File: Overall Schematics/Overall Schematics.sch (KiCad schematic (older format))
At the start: 33 parts, among them J1 WattMeter1_Output, J2 WattMeter2_Output, J3 Intel_Buck_Converter_Input, J4 WattMeter1_Input, J5 WattMeter2_Input, M1 Stepper_Motor_bipolar, M10 Motor_Servo, M11 Stepper_Motor_bipolar, M12 Motor_Servo, M2 Stepper_Motor_bipolar, M3 LinActuator12V, M4 LinActuator12V, M5 LinActuator12V, M6 Motor_DC, M7 Motor_DC, M8 Motor_DC, M9 Motor_DC, SW1 SW_DPST, U1 Teensy4.1, U10 VNH52019, U11 ServoDriver, U12 36v4SMD, U13 D24V22F5, U2 36v4SMD, U3 36v4SMD, U4 VNH52019, U5 VNH52019, U6 VNH52019, U7 VNH52019, U8 VNH52019, U9 VNH52019

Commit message: PCB is basically done, going to check stuff again before ordering though
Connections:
- net Battery2_Positive is gone; now on net Battery2_Positive24V: J3.1 (Pin_1)
- net Battery1_Positive24V: now also U12.17 (VIN), U12.18 (VIN2), U5.14 (VIN(5.5V-24V)); no longer U10.14 (VIN(5.5V-24V)), U3.17 (VIN), U3.18 (VIN2)
- net Battery2_Positive24V: now also U10.14 (VIN(5.5V-24V)), U3.17 (VIN), U3.18 (VIN2); no longer U12.17 (VIN), U12.18 (VIN2), U5.14 (VIN(5.5V-24V))
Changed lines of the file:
@@
 	20950 12700 21050 12700
-$Comp
-L power:+3V3 #PWR0105
-U 1 1 5FAD46F5
-P 21050 12800
-F 0 "#PWR0105" H 21050 12650 50  0001 C CNN
-F 1 "+3V3" V 21065 12928 50  0000 L CNN
-F 2 "" H 21050 12800 50  0001 C CNN
-F 3 "" H 21050 12800 50  0001 C CNN
-	1    21050 12800
-	0    1    1    0
-$EndComp
-Wire Wire Line
-	20950 12800 21050 12800
 $Comp
 L power:+3V3 #PWR0106
@@
 Text GLabel 27400 15250 2    20   Input ~ 0
 Battery2_Positive24V
-Text GLabel 28750 14750 0    39   Input ~ 0
-Battery2_Positive
 Text GLabel 28550 12700 2    39   Input ~ 0
-Battery1_Positive24V
+Battery2_Positive24V
 Wire Wire Line
 	28400 11850 28550 11850
 Text GLabel 28550 11850 2    39   Input ~ 0
 Battery1_Positive24V
-Text GLabel 28550 11050 2    39   Input ~ 0
-Battery2_Positive24V
 Text GLabel 23600 11600 2    39   Input ~ 0
-Battery1_Positive24V
-Text GLabel 23550 10550 2    39   Input ~ 0
-Battery2_Positive24V
-Text GLabel 28550 10350 2    39   Input ~ 0
 Battery2_Positive24V
 Text GLabel 29500 9650 1    31   Input ~ 0
@@
 Battery1_Positive24V
 Text GLabel 23700 16750 2    39   Input ~ 0
-Battery2_Positive24V
+Battery1_Positive24V
 Wire Wire Line
 	23600 15400 23600 15500
@@
 	23600 9500 23600 9450
 Text GLabel 23600 9450 2    20   Input ~ 0
-Battery2_Positive24V
+Battery1_Positive24V
 Text GLabel 23600 9600 2    20   Input ~ 0
 PWR_GND
@@
 	0    1    1    0
 $EndComp
+$Comp
+L power:+3V3 #PWR0105
+U 1 1 602D660B
+P 21250 12800
+F 0 "#PWR0105" H 21250 12650 50  0001 C CNN
+F 1 "+3V3" H 21265 12973 50  0000 C CNN
+F 2 "" H 21250 12800 50  0001 C CNN
+F 3 "" H 21250 12800 50  0001 C CNN
+	1    21250 12800
+	0    1    1    0
+$EndComp
+Wire Wire Line
+	20950 12800 21250 12800
+Text GLabel 28750 14750 0    20   Input ~ 0
+Battery2_Positive24V
+Text GLabel 28550 11050 2    39   Input ~ 0
+Battery2_Positive24V
+Text GLabel 28550 10350 2    39   Input ~ 0
+Battery2_Positive24V
+Text GLabel 23550 10550 2    39   Input ~ 0
+Battery2_Positive24V
 $EndSCHEMATC

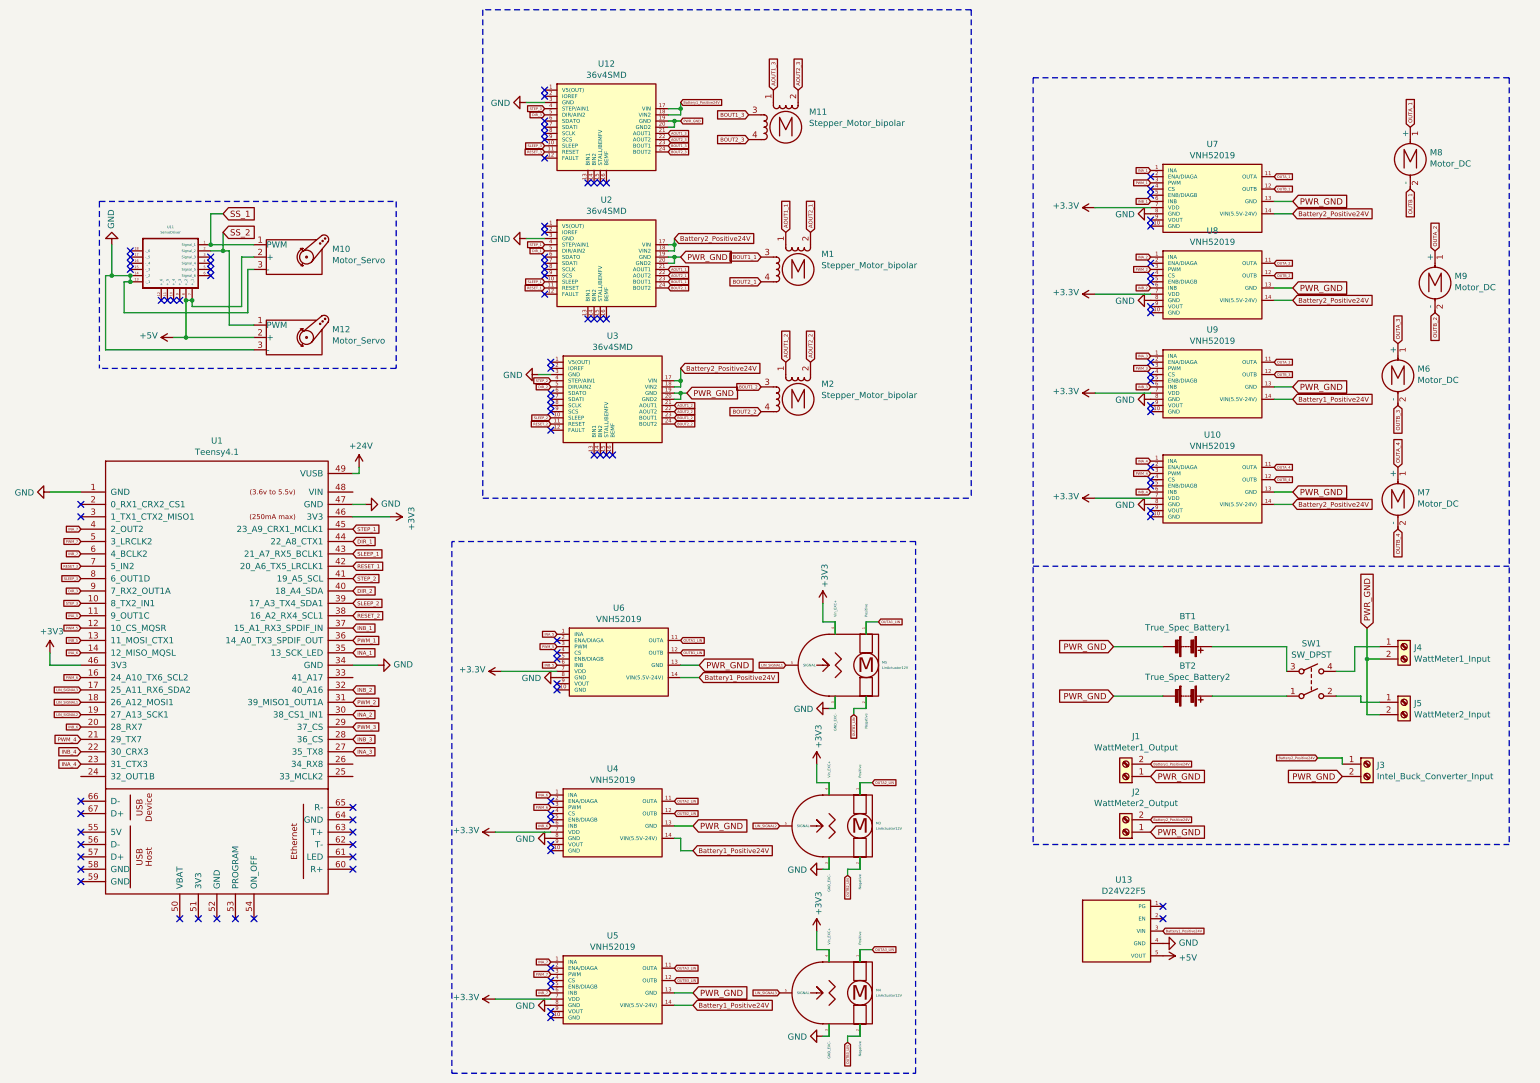
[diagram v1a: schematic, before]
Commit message: Added mounting, add to make board a bit bigger. Changed servo screw terminal pitch to 2.54mm
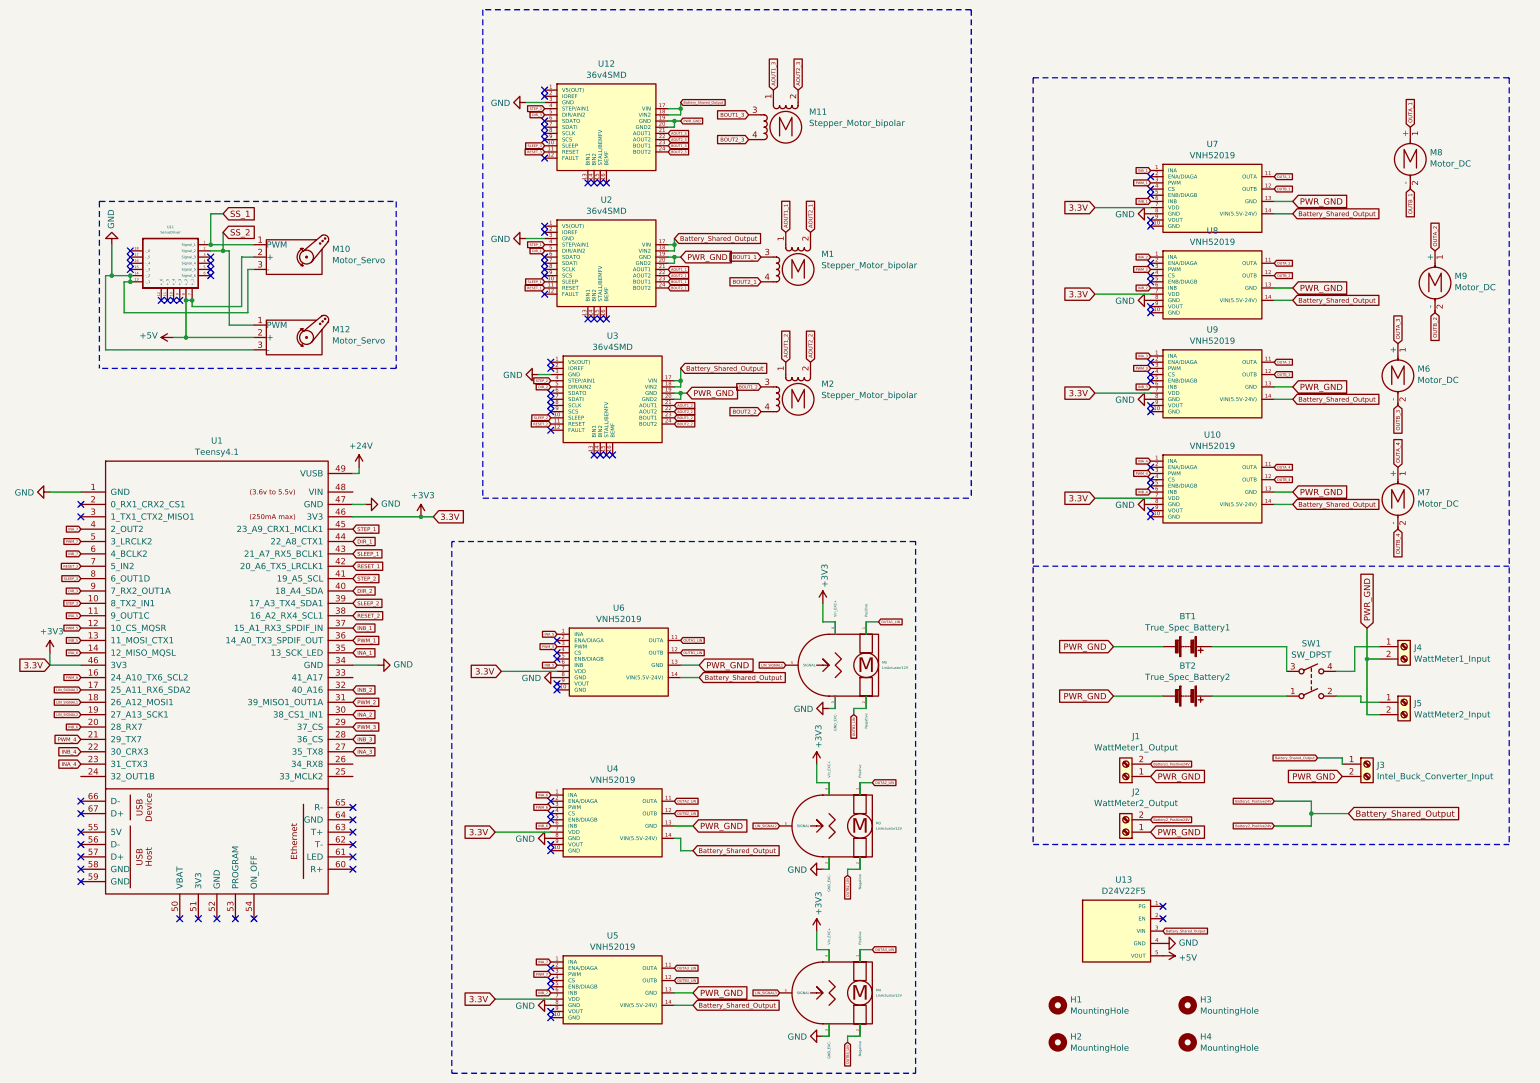
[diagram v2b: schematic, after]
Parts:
- added H1, H2, H3, H4: MountingHole, MountingHole:MountingHole_3.2mm_M3, symbol Mechanical:MountingHole
- M10, M12: footprint TerminalBlock:TerminalBlock_bornier-3_P5.08mm -> Custom Footprints:TerminalBlock_2.54_1x03_P2.54mm_Horizontal
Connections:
- net Battery2_Positive24V is gone; now on net Battery1_Positive24V: J2.2 (Pin_2), J3.1 (Pin_1), U10.14 (VIN(5.5V-24V)), U2.17 (VIN), U2.18 (VIN2), U3.17 (VIN), U3.18 (VIN2), U7.14 (VIN(5.5V-24V)), U8.14 (VIN(5.5V-24V))
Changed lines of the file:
@@
 Wire Wire Line
 	27400 12650 26950 12650
-$Comp
-L power:+3.3V #PWR0113
-U 1 1 5FB92EE3
-P 26950 12650
-F 0 "#PWR0113" H 26950 12500 50  0001 C CNN
-F 1 "+3.3V" V 26965 12778 50  0000 L CNN
-F 2 "" H 26950 12650 50  0001 C CNN
-F 3 "" H 26950 12650 50  0001 C CNN
-	1    26950 12650
-	0    -1   -1   0
-$EndComp
 NoConn ~ 27400 12800
 NoConn ~ 27400 12750
@@
 Wire Wire Line
 	27400 11800 26950 11800
-$Comp
-L power:+3.3V #PWR0114
-U 1 1 5FBBE25C
-P 26950 11800
-F 0 "#PWR0114" H 26950 11650 50  0001 C CNN
-F 1 "+3.3V" V 26965 11928 50  0000 L CNN
-F 2 "" H 26950 11800 50  0001 C CNN
-F 3 "" H 26950 11800 50  0001 C CNN
-	1    26950 11800
-	0    -1   -1   0
-$EndComp
 NoConn ~ 27400 11700
 NoConn ~ 27400 11650
@@
 Wire Wire Line
 	27400 11000 26950 11000
-$Comp
-L power:+3.3V #PWR0115
-U 1 1 5FBE8F2B
-P 26950 11000
-F 0 "#PWR0115" H 26950 10850 50  0001 C CNN
-F 1 "+3.3V" V 26965 11128 50  0000 L CNN
-F 2 "" H 26950 11000 50  0001 C CNN
-F 3 "" H 26950 11000 50  0001 C CNN
-	1    26950 11000
-	0    -1   -1   0
-$EndComp
 NoConn ~ 27400 10850
 NoConn ~ 27400 11100
@@
 Wire Wire Line
 	27400 10300 26950 10300
-$Comp
-L power:+3.3V #PWR0116
-U 1 1 5FC56265
-P 26950 10300
-F 0 "#PWR0116" H 26950 10150 50  0001 C CNN
-F 1 "+3.3V" V 26965 10428 50  0000 L CNN
-F 2 "" H 26950 10300 50  0001 C CNN
-F 3 "" H 26950 10300 50  0001 C CNN
-	1    26950 10300
-	0    -1   -1   0
-$EndComp
 NoConn ~ 27400 10400
 NoConn ~ 27400 10450
@@
 Wire Wire Line
 	22600 14050 22150 14050
-$Comp
-L power:+3.3V #PWR0118
-U 1 1 5FAB3F63
-P 22150 14050
-F 0 "#PWR0118" H 22150 13900 50  0001 C CNN
-F 1 "+3.3V" V 22165 14178 50  0000 L CNN
-F 2 "" H 22150 14050 50  0001 C CNN
-F 3 "" H 22150 14050 50  0001 C CNN
-	1    22150 14050
-	0    -1   -1   0
-$EndComp
 NoConn ~ 22600 14200
 NoConn ~ 22600 14150
@@
 Wire Wire Line
 	22550 15350 22100 15350
-$Comp
-L power:+3.3V #PWR0122
-U 1 1 5FAE49B6
-P 22100 15350
-F 0 "#PWR0122" H 22100 15200 50  0001 C CNN
-F 1 "+3.3V" V 22115 15478 50  0000 L CNN
-F 2 "" H 22100 15350 50  0001 C CNN
-F 3 "" H 22100 15350 50  0001 C CNN
-	1    22100 15350
-	0    -1   -1   0
-$EndComp
 NoConn ~ 22550 15500
 NoConn ~ 22550 15450
@@
 Wire Wire Line
 	22550 16700 22100 16700
-$Comp
-L power:+3.3V #PWR0126
-U 1 1 5FB0E62E
-P 22100 16700
-F 0 "#PWR0126" H 22100 16550 50  0001 C CNN
-F 1 "+3.3V" V 22115 16828 50  0000 L CNN
-F 2 "" H 22100 16700 50  0001 C CNN
-F 3 "" H 22100 16700 50  0001 C CNN
-	1    22100 16700
-	0    -1   -1   0
-$EndComp
 NoConn ~ 22550 16850
 NoConn ~ 22550 16800
@@
 Battery2_Positive24V
 Text GLabel 28550 12700 2    39   Input ~ 0
-Battery2_Positive24V
+Battery_Shared_Output
 Wire Wire Line
 	28400 11850 28550 11850
 Text GLabel 28550 11850 2    39   Input ~ 0
-Battery1_Positive24V
+Battery_Shared_Output
 Text GLabel 23600 11600 2    39   Input ~ 0
-Battery2_Positive24V
+Battery_Shared_Output
 Text GLabel 29500 9650 1    31   Input ~ 0
 OUTA_1
 Text GLabel 23750 14100 2    39   Input ~ 0
-Battery1_Positive24V
+Battery_Shared_Output
 Text GLabel 23700 15500 2    39   Input ~ 0
-Battery1_Positive24V
+Battery_Shared_Output
 Text GLabel 23700 16750 2    39   Input ~ 0
-Battery1_Positive24V
+Battery_Shared_Output
 Wire Wire Line
 	23600 15400 23600 15500
@@
 	23600 9500 23600 9450
 Text GLabel 23600 9450 2    20   Input ~ 0
-Battery1_Positive24V
+Battery_Shared_Output
 Text GLabel 23600 9600 2    20   Input ~ 0
 PWR_GND
@@
 F 0 "M10" H 20782 10765 50  0000 L CNN
 F 1 "Motor_Servo" H 20782 10674 50  0000 L CNN
-F 2 "TerminalBlock:TerminalBlock_bornier-3_P5.08mm" H 20450 10510 50  0001 C CNN
+F 2 "Custom Footprints:TerminalBlock_2.54_1x03_P2.54mm_Horizontal" H 20450 10510 50  0001 C CNN
 F 3 "http://forums.parallax.com/uploads/attachments/46831/74481.png" H 20450 10510 50  0001 C CNN
 	1    20450 10700
@@
 F 0 "M12" H 20782 11415 50  0000 L CNN
 F 1 "Motor_Servo" H 20782 11324 50  0000 L CNN
-F 2 "TerminalBlock:TerminalBlock_bornier-3_P5.08mm" H 20450 11160 50  0001 C CNN
+F 2 "Custom Footprints:TerminalBlock_2.54_1x03_P2.54mm_Horizontal" H 20450 11160 50  0001 C CNN
 F 3 "http://forums.parallax.com/uploads/attachments/46831/74481.png" H 20450 11160 50  0001 C CNN
 	1    20450 11350
@@
 $EndComp
 Text GLabel 27500 16150 2    20   Input ~ 0
-Battery1_Positive24V
+Battery_Shared_Output
 $Comp
 L power:+5V #PWR04
@@
 L power:+3V3 #PWR0105
 U 1 1 602D660B
-P 21250 12800
-F 0 "#PWR0105" H 21250 12650 50  0001 C CNN
-F 1 "+3V3" H 21265 12973 50  0000 C CNN
-F 2 "" H 21250 12800 50  0001 C CNN
-F 3 "" H 21250 12800 50  0001 C CNN
-	1    21250 12800
-	0    1    1    0
-$EndComp
-Wire Wire Line
-	20950 12800 21250 12800
+P 21500 12800
+F 0 "#PWR0105" H 21500 12650 50  0001 C CNN
+F 1 "+3V3" H 21515 12973 50  0000 C CNN
+F 2 "" H 21500 12800 50  0001 C CNN
+F 3 "" H 21500 12800 50  0001 C CNN
+	1    21500 12800
+	1    0    0    -1
+$EndComp
 Text GLabel 28750 14750 0    20   Input ~ 0
+Battery_Shared_Output
+Text GLabel 28550 11050 2    39   Input ~ 0
+Battery_Shared_Output
+Text GLabel 28550 10350 2    39   Input ~ 0
+Battery_Shared_Output
+Text GLabel 23550 10550 2    39   Input ~ 0
+Battery_Shared_Output
+Text GLabel 29000 15200 2    50   Input ~ 0
+Battery_Shared_Output
+Wire Wire Line
+	29000 15200 28700 15200
+Wire Wire Line
+	28700 15200 28700 15100
+Wire Wire Line
+	28700 15100 28400 15100
+Wire Wire Line
+	28700 15200 28700 15300
+Wire Wire Line
+	28700 15300 28400 15300
+Connection ~ 28700 15200
+Text GLabel 28400 15100 0    20   Input ~ 0
+Battery1_Positive24V
+Text GLabel 28400 15300 0    20   Input ~ 0
 Battery2_Positive24V
-Text GLabel 28550 11050 2    39   Input ~ 0
-Battery2_Positive24V
-Text GLabel 28550 10350 2    39   Input ~ 0
-Battery2_Positive24V
-Text GLabel 23550 10550 2    39   Input ~ 0
-Battery2_Positive24V
+$Comp
+L Mechanical:MountingHole H1
+U 1 1 601D065D
+P 26650 16750
+F 0 "H1" H 26750 16796 50  0000 L CNN
+F 1 "MountingHole" H 26750 16705 50  0000 L CNN
+F 2 "MountingHole:MountingHole_3.2mm_M3" H 26650 16750 50  0001 C CNN
+F 3 "~" H 26650 16750 50  0001 C CNN
+	1    26650 16750
+	1    0    0    -1
+$EndComp
+$Comp
+L Mechanical:MountingHole H2
+U 1 1 601D19D9
+P 26650 17050
+F 0 "H2" H 26750 17096 50  0000 L CNN
+F 1 "MountingHole" H 26750 17005 50  0000 L CNN
+F 2 "MountingHole:MountingHole_3.2mm_M3" H 26650 17050 50  0001 C CNN
+F 3 "~" H 26650 17050 50  0001 C CNN
+	1    26650 17050
+	1    0    0    -1
+$EndComp
+$Comp
+L Mechanical:MountingHole H3
+U 1 1 601D7CC2
+P 27700 16750
+F 0 "H3" H 27800 16796 50  0000 L CNN
+F 1 "MountingHole" H 27800 16705 50  0000 L CNN
+F 2 "MountingHole:MountingHole_3.2mm_M3" H 27700 16750 50  0001 C CNN
+F 3 "~" H 27700 16750 50  0001 C CNN
+	1    27700 16750
+	1    0    0    -1
+$EndComp
+$Comp
+L Mechanical:MountingHole H4
+U 1 1 601D7CC8
+P 27700 17050
+F 0 "H4" H 27800 17096 50  0000 L CNN
+F 1 "MountingHole" H 27800 17005 50  0000 L CNN
+F 2 "MountingHole:MountingHole_3.2mm_M3" H 27700 17050 50  0001 C CNN
+F 3 "~" H 27700 17050 50  0001 C CNN
+	1    27700 17050
+	1    0    0    -1
+$EndComp
+Text GLabel 18500 14000 0    50   Input ~ 0
+3.3V
+Text GLabel 21600 12800 2    50   Input ~ 0
+3.3V
+Wire Wire Line
+	20950 12800 21500 12800
+Wire Wire Line
+	21500 12800 21600 12800
+Connection ~ 21500 12800
+Text GLabel 22150 14050 0    50   Input ~ 0
+3.3V
+Text GLabel 22100 15350 0    50   Input ~ 0
+3.3V
+Text GLabel 22100 16700 0    50   Input ~ 0
+3.3V
+Text GLabel 26950 12650 0    50   Input ~ 0
+3.3V
+Text GLabel 26950 11800 0    50   Input ~ 0
+3.3V
+Text GLabel 26950 11000 0    50   Input ~ 0
+3.3V
+Text GLabel 26950 10300 0    50   Input ~ 0
+3.3V
 $EndSCHEMATC
